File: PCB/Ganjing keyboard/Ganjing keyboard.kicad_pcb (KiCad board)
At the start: 2 copper layers, 304.8 x 122.8 mm, 172 parts, among them J1 Conn_01x04, J2 AVR-ISP-6, SW1 Rotary_Encoder_Switch, U1 ATmega32A-PU, Y1 Crystal

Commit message: Almost done routing clean up
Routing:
- net Net-(D48-Pad2): track 127.1 -> 130.2 mm

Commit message: Updating packages and reducing empty copper pours
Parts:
- moved C2 0.15 mm to (132.0, 121.7)
- moved C3 0.15 mm to (124.5, 119.2)
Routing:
- net Net-(D6-Pad2): track 87.6 -> 92.6 mm
- net Boot: track 114.4 -> 118.3 mm
- net Net-(D21-Pad2): track 66.7 -> 70.2 mm
- net row4: track 401.0 -> 404.3 mm
- net B1: track 295.2 -> 298.3 mm
- net B2: track 291.6 -> 294.5 mm
- net Net-(D41-Pad2): track 74.3 -> 71.7 mm
- net col13: track 302.1 -> 304.3 mm
- net col12: track 258.7 -> 260.9 mm
- net col11: track 254.8 -> 257.0 mm
- net col10: track 206.4 -> 208.6 mm
- net col9: track 246.2 -> 248.3 mm
- net col8: track 225.7 -> 227.8 mm
- net col7: track 197.3 -> 199.3 mm
- net col5: track 167.4 -> 169.5 mm
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
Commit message: Added remaining mounting holes
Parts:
- added REF10: MountingHole_2.2mm_M2_Pad, Keyboard:MountingHole_2.2mm_M2_Pad, F.Cu at (211.9, 205.6)
- added REF11: MountingHole_2.2mm_M2_Pad, Keyboard:MountingHole_2.2mm_M2_Pad, F.Cu at (304.6, 142.9)
- added REF12: MountingHole_2.2mm_M2_Pad, Keyboard:MountingHole_2.2mm_M2_Pad, F.Cu at (321.6, 199.7)
- added REF4: MountingHole_2.2mm_M2_Pad, Keyboard:MountingHole_2.2mm_M2_Pad, F.Cu at (0.00, 159.8)
- added REF7: MountingHole_2.2mm_M2_Pad, Keyboard:MountingHole_2.2mm_M2_Pad, F.Cu at (119.5, 142.9)
- added REF8: MountingHole_2.2mm_M2_Pad, Keyboard:MountingHole_2.2mm_M2_Pad, F.Cu at (102.3, 199.7)
- added REF9: MountingHole_2.2mm_M2_Pad, Keyboard:MountingHole_2.2mm_M2_Pad, F.Cu at (211.9, 142.9)
- moved D64 1.60 mm to (318.8, 198.6)
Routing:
- net Net-(D50-Pad2): track 111.8 -> 125.3 mm
- net Net-(D46-Pad2): track 143.1 -> 135.7 mm
- net Net-(D33-Pad2): track 112.5 -> 105.3 mm
- net row4: track 404.3 -> 405.9 mm
- net Net-(D64-Pad2): track 8.02 -> 9.62 mm

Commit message: Done adding via stitching
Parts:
- removed the REF4 at (0.00, 159.8)
- D68: value Caps lock -> Caps
- USB1: value USB_C_GCT_USB4085 -> USB_C_USB4085
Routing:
- net Net-(D17-Pad2): track 87.8 -> 93.1 mm
- net Net-(D32-Pad2): track 105.1 -> 108.9 mm
- net Net-(D67-Pad2): track 138.7 -> 142.5 mm
- net col8: track 227.8 -> 229.7 mm
- net col5: track 169.5 -> 171.4 mm
- net col9: track 248.3 -> 250.2 mm
- net col7: track 199.3 -> 201.3 mm
- net col4: track 145.0 -> 146.9 mm
- net col10: track 208.6 -> 210.5 mm
- net col11: track 257.0 -> 258.9 mm
- net Net-(D31-Pad2): track 138.3 -> 140.2 mm
- net col3: track 125.4 -> 127.2 mm
- net col6: track 222.9 -> 224.8 mm
- net col1: track 150.1 -> 148.8 mm
- net col2: track 136.7 -> 135.4 mm
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
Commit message: Changing footprint for crystal and adding some silk screen text
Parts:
- D68: value Caps -> Caps lock
- USB1: value USB_C_USB4085 -> USB_C_GCT_USB4085
- Y1: footprint Keyboard:Crystal_HC49-4H_Vertical -> GanJing-crystal:CTS-ATS16B-0
- moved Y1 2.35 mm to (139.3, 120.4)
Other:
- board text added: "Designed by Mingze Jin"
- board text added: "GanJing Keyboard prototype"

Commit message: Fixing some silk screen stuff on the PCB
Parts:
- D68: value Caps lock -> Caps
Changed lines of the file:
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@@
     (add_net row4)
   )
+  (module Rotary_Encoder:RotaryEncoder_Alps_EC11E-Switch_Vertical_H20mm (layer F.Cu)
+    (at 352.425 140.49375 90)
+    (descr "Alps rotary encoder, EC12E... with switch, vertical shaft, http://www.alps.com/prod/info/E/HTML/Encoder/Incremental/EC11/EC11E15204A3.html")
+    (tags "rotary encoder")
+    (fp_text reference SW1 (at 2.8 -4.7 90) (layer F.SilkS)
+      (effects (font (size 1 1) (thickness 0.15)))
+    )
+    (fp_text value Rotary_Encoder_Switch (at 7.5 10.4 90) (layer F.Fab)
+      (effects (font (size 1 1) (thickness 0.15)))
+    )
+    (fp_circle (center 7.5 2.5) (end 10.5 2.5) (layer F.Fab) (width 0.12))
+    (fp_circle (center 7.5 2.5) (end 10.5 2.5) (layer F.Fab) (width 0.12))
+    (fp_line (start 16 9.6) (end -1.5 9.6) (layer F.CrtYd) (width 0.05))
+    (fp_line (start 16 9.6) (end 16 -4.6) (layer F.CrtYd) (width 0.05))
+    (fp_line (start -1.5 -4.6) (end -1.5 9.6) (layer F.CrtYd) (width 0.05))
+    (fp_line (start -1.5 -4.6) (end 16 -4.6) (layer F.CrtYd) (width 0.05))
+    (fp_line (start 2.5 -3.3) (end 13.5 -3.3) (layer F.Fab) (width 0.12))
+    (fp_line (start 13.5 -3.3) (end 13.5 8.3) (layer F.Fab) (width 0.12))
+    (fp_line (start 13.5 8.3) (end 1.5 8.3) (layer F.Fab) (width 0.12))
+    (fp_line (start 1.5 8.3) (end 1.5 -2.2) (layer F.Fab) (width 0.12))
+    (fp_line (start 1.5 -2.2) (end 2.5 -3.3) (layer F.Fab) (width 0.12))
+    (fp_line (start 9.5 -3.4) (end 13.6 -3.4) (layer F.Fab) (width 0.12))
+    (fp_line (start 13.6 8.4) (end 9.5 8.4) (layer F.Fab) (width 0.12))
+    (fp_line (start 5.5 8.4) (end 1.4 8.4) (layer F.Fab) (width 0.12))
+    (fp_line (start 5.5 -3.4) (end 1.4 -3.4) (layer F.Fab) (width 0.12))
+    (fp_line (start 1.4 -3.4) (end 1.4 8.4) (layer F.Fab) (width 0.12))
+    (fp_line (start 0 -1.3) (end -0.3 -1.6) (layer F.SilkS) (width 0.12))
+    (fp_line (start -0.3 -1.6) (end 0.3 -1.6) (layer F.SilkS) (width 0.12))
+    (fp_line (start 0.3 -1.6) (end 0 -1.3) (layer F.SilkS) (width 0.12))
+    (fp_line (start 7.5 -0.5) (end 7.5 5.5) (layer F.Fab) (width 0.12))
+    (fp_line (start 4.5 2.5) (end 10.5 2.5) (layer F.Fab) (width 0.12))
+    (fp_line (start 13.6 -3.4) (end 13.6 -1) (layer F.Fab) (width 0.12))
+    (fp_line (start 13.6 1.2) (end 13.6 3.8) (layer F.Fab) (width 0.12))
+    (fp_line (start 13.6 6) (end 13.6 8.4) (layer F.Fab) (width 0.12))
+    (fp_line (start 7.5 2) (end 7.5 3) (layer F.Fab) (width 0.12))
+    (fp_line (start 7 2.5) (end 8 2.5) (layer F.Fab) (width 0.12))
+    (fp_text user %R (at 11.1 6.3 90) (layer F.Fab)
+      (effects (font (size 1 1) (thickness 0.15)))
+    )
+    (pad A thru_hole rect (at 0 0 90) (size 2 2) (drill 1) (layers *.Cu *.Mask)
+      (net 111 B2))
+    (pad C thru_hole circle (at 0 2.5 90) (size 2 2) (drill 1) (layers *.Cu *.Mask)
+      (net 1 GND))
+    (pad B thru_hole circle (at 0 5 90) (size 2 2) (drill 1) (layers *.Cu *.Mask)
+      (net 112 B1))
+    (pad MP thru_hole rect (at 7.5 -3.1 90) (size 3.2 2) (drill oval 2.8 1.5) (layers *.Cu *.Mask))
+    (pad MP thru_hole rect (at 7.5 8.1 90) (size 3.2 2) (drill oval 2.8 1.5) (layers *.Cu *.Mask))
+    (pad S2 thru_hole circle (at 14.5 0 90) (size 2 2) (drill 1) (layers *.Cu *.Mask)
+      (net 20 SW15B))
+    (pad S1 thru_hole circle (at 14.5 5 90) (size 2 2) (drill 1) (layers *.Cu *.Mask)
+      (net 103 SW15A))
+    (model ${KISYS3DMOD}/Rotary_Encoder.3dshapes/RotaryEncoder_Alps_EC11E-Switch_Vertical_H20mm.wrl
+      (at (xyz 0 0 0))
+      (scale (xyz 1 1 1))
+      (rotate (xyz 0 0 0))
+    )
+  )
+  (module "Keyboard:ssd1306 128x32 oled" (layer F.Cu)
+    (at 269.08125 209.55)
+    (fp_text reference J1 (at 0 0.5) (layer F.SilkS)
+      (effects (font (size 1 1) (thickness 0.15)))
+    )
+    (fp_text value Conn_01x04 (at 0 -0.5) (layer F.Fab)
+      (effects (font (size 1 1) (thickness 0.15)))
+    )
+    (fp_line (start -14 6) (end -14 -6) (layer F.Fab) (width 0.15))
+    (fp_line (start 19 6) (end 19 -6) (layer F.Fab) (width 0.15))
+    (fp_line (start -19 6) (end -19 -6) (layer F.Fab) (width 0.15))
+    (fp_line (start -19 6) (end 19 6) (layer F.Fab) (width 0.15))
+    (fp_line (start -19 -6) (end 19 -6) (layer F.Fab) (width 0.15))
+    (pad 1 thru_hole circle (at -17.5 3.81) (size 1.524 1.524) (drill 0.762) (layers *.Cu *.Mask)
+      (net 83 SDA))
+    (pad 2 thru_hole circle (at -17.5 1.27) (size 1.524 1.524) (drill 0.762) (layers *.Cu *.Mask)
+      (net 84 SCL))
+    (pad 3 thru_hole circle (at -17.5 -1.27) (size 1.524 1.524) (drill 0.762) (layers *.Cu *.Mask)
+      (net 82 VCC))
+    (pad 4 thru_hole circle (at -17.5 -3.81) (size 1.524 1.524) (drill 0.762) (layers *.Cu *.Mask)
+      (net 1 GND))
+  )
   (module GanJing-crystal:CTS-ATS16B-0 (layer F.Cu)
     (at 139.3 120.4 180)
@@
     (pad 1 thru_hole circle (at 0 0) (size 4.4 4.4) (drill 2.2) (layers *.Cu *.Mask))
   )
-  (module Rotary_Encoder:RotaryEncoder_Alps_EC11E-Switch_Vertical_H20mm (layer F.Cu)
-    (at 352.425 140.49375 90)
-    (descr "Alps rotary encoder, EC12E... with switch, vertical shaft, http://www.alps.com/prod/info/E/HTML/Encoder/Incremental/EC11/EC11E15204A3.html")
-    (tags "rotary encoder")
-    (fp_text reference SW1 (at 2.8 -4.7 90) (layer F.SilkS)
-      (effects (font (size 1 1) (thickness 0.15)))
-    )
-    (fp_text value Rotary_Encoder_Switch (at 7.5 10.4 90) (layer F.Fab)
-      (effects (font (size 1 1) (thickness 0.15)))
-    )
-    (fp_circle (center 7.5 2.5) (end 10.5 2.5) (layer F.Fab) (width 0.12))
-    (fp_circle (center 7.5 2.5) (end 10.5 2.5) (layer F.SilkS) (width 0.12))
-    (fp_line (start 16 9.6) (end -1.5 9.6) (layer F.CrtYd) (width 0.05))
-    (fp_line (start 16 9.6) (end 16 -4.6) (layer F.CrtYd) (width 0.05))
-    (fp_line (start -1.5 -4.6) (end -1.5 9.6) (layer F.CrtYd) (width 0.05))
-    (fp_line (start -1.5 -4.6) (end 16 -4.6) (layer F.CrtYd) (width 0.05))
-    (fp_line (start 2.5 -3.3) (end 13.5 -3.3) (layer F.Fab) (width 0.12))
-    (fp_line (start 13.5 -3.3) (end 13.5 8.3) (layer F.Fab) (width 0.12))
-    (fp_line (start 13.5 8.3) (end 1.5 8.3) (layer F.Fab) (width 0.12))
-    (fp_line (start 1.5 8.3) (end 1.5 -2.2) (layer F.Fab) (width 0.12))
-    (fp_line (start 1.5 -2.2) (end 2.5 -3.3) (layer F.Fab) (width 0.12))
-    (fp_line (start 9.5 -3.4) (end 13.6 -3.4) (layer F.SilkS) (width 0.12))
-    (fp_line (start 13.6 8.4) (end 9.5 8.4) (layer F.SilkS) (width 0.12))
-    (fp_line (start 5.5 8.4) (end 1.4 8.4) (layer F.SilkS) (width 0.12))
-    (fp_line (start 5.5 -3.4) (end 1.4 -3.4) (layer F.SilkS) (width 0.12))
-    (fp_line (start 1.4 -3.4) (end 1.4 8.4) (layer F.SilkS) (width 0.12))
-    (fp_line (start 0 -1.3) (end -0.3 -1.6) (layer F.SilkS) (width 0.12))
-    (fp_line (start -0.3 -1.6) (end 0.3 -1.6) (layer F.SilkS) (width 0.12))
-    (fp_line (start 0.3 -1.6) (end 0 -1.3) (layer F.SilkS) (width 0.12))
-    (fp_line (start 7.5 -0.5) (end 7.5 5.5) (layer F.Fab) (width 0.12))
-    (fp_line (start 4.5 2.5) (end 10.5 2.5) (layer F.Fab) (width 0.12))
-    (fp_line (start 13.6 -3.4) (end 13.6 -1) (layer F.SilkS) (width 0.12))
-    (fp_line (start 13.6 1.2) (end 13.6 3.8) (layer F.SilkS) (width 0.12))
-    (fp_line (start 13.6 6) (end 13.6 8.4) (layer F.SilkS) (width 0.12))
-    (fp_line (start 7.5 2) (end 7.5 3) (layer F.SilkS) (width 0.12))
-    (fp_line (start 7 2.5) (end 8 2.5) (layer F.SilkS) (width 0.12))
-    (fp_text user %R (at 11.1 6.3 90) (layer F.Fab)
-      (effects (font (size 1 1) (thickness 0.15)))
-    )
-    (pad A thru_hole rect (at 0 0 90) (size 2 2) (drill 1) (layers *.Cu *.Mask)
-      (net 111 B2))
-    (pad C thru_hole circle (at 0 2.5 90) (size 2 2) (drill 1) (layers *.Cu *.Mask)
-      (net 1 GND))
-    (pad B thru_hole circle (at 0 5 90) (size 2 2) (drill 1) (layers *.Cu *.Mask)
-      (net 112 B1))
-    (pad MP thru_hole rect (at 7.5 -3.1 90) (size 3.2 2) (drill oval 2.8 1.5) (layers *.Cu *.Mask))
-    (pad MP thru_hole rect (at 7.5 8.1 90) (size 3.2 2) (drill oval 2.8 1.5) (layers *.Cu *.Mask))
-    (pad S2 thru_hole circle (at 14.5 0 90) (size 2 2) (drill 1) (layers *.Cu *.Mask)
-      (net 20 SW15B))
-    (pad S1 thru_hole circle (at 14.5 5 90) (size 2 2) (drill 1) (layers *.Cu *.Mask)
-      (net 103 SW15A))
-    (model ${KISYS3DMOD}/Rotary_Encoder.3dshapes/RotaryEncoder_Alps_EC11E-Switch_Vertical_H20mm.wrl
-      (at (xyz 0 0 0))
-      (scale (xyz 1 1 1))
-      (rotate (xyz 0 0 0))
-    )
-  )
   (module MX_Only:MXOnly-1.5U-NoLED (layer F.Cu)
     (at 330.99375 152.4)
@@
     )
   )
-  (module "Keyboard:ssd1306 128x32 oled" (layer F.Cu)
-    (at 269.08125 209.55)
-    (fp_text reference J1 (at 0 0.5) (layer F.SilkS)
-      (effects (font (size 1 1) (thickness 0.15)))
-    )
-    (fp_text value Conn_01x04 (at 0 -0.5) (layer F.Fab)
-      (effects (font (size 1 1) (thickness 0.15)))
-    )
-    (fp_line (start -14 6) (end -14 -6) (layer F.SilkS) (width 0.15))
-    (fp_line (start 19 6) (end 19 -6) (layer F.SilkS) (width 0.15))
-    (fp_line (start -19 6) (end -19 -6) (layer F.SilkS) (width 0.15))
-    (fp_line (start -19 6) (end 19 6) (layer F.SilkS) (width 0.15))
-    (fp_line (start -19 -6) (end 19 -6) (layer F.SilkS) (width 0.15))
-    (pad 1 thru_hole circle (at -17.5 3.81) (size 1.524 1.524) (drill 0.762) (layers *.Cu *.Mask)
-      (net 83 SDA))
-    (pad 2 thru_hole circle (at -17.5 1.27) (size 1.524 1.524) (drill 0.762) (layers *.Cu *.Mask)
-      (net 84 SCL))
-    (pad 3 thru_hole circle (at -17.5 -1.27) (size 1.524 1.524) (drill 0.762) (layers *.Cu *.Mask)
-      (net 82 VCC))
-    (pad 4 thru_hole circle (at -17.5 -3.81) (size 1.524 1.524) (drill 0.762) (layers *.Cu *.Mask)
-      (net 1 GND))
-  )
   (module Keyboard:polyfuse_5.1mm (layer F.Cu)
     (at 84.2 112)
@@
       (effects (font (size 1 1) (thickness 0.15)))
     )
-    (fp_text value "Caps lock" (at 7.5 -1.1) (layer F.SilkS)
+    (fp_text value Caps (at 7.5 -1.1) (layer F.SilkS)
       (effects (font (size 1.5 1.5) (thickness 0.25)))
     )

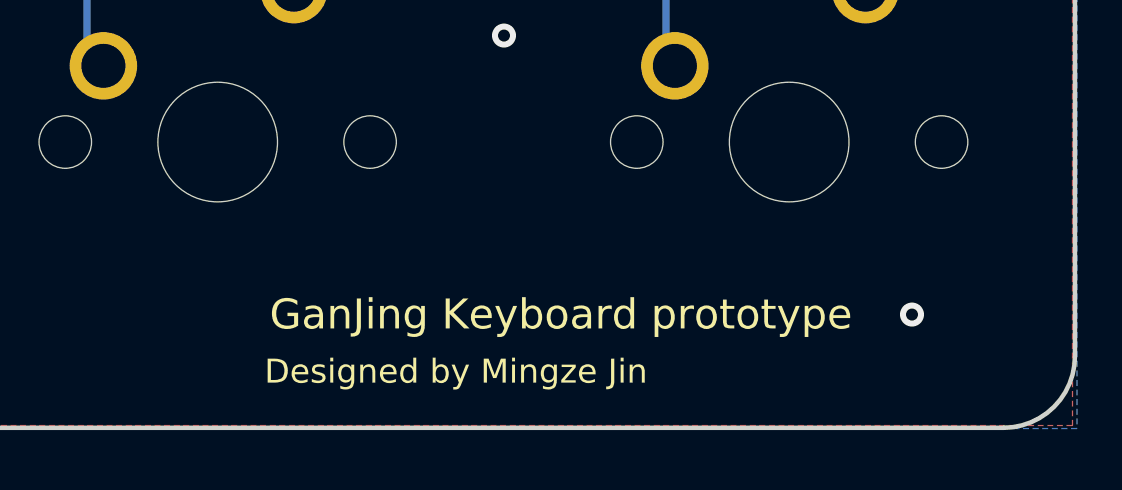
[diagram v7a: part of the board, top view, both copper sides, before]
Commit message: Minor mistake in text
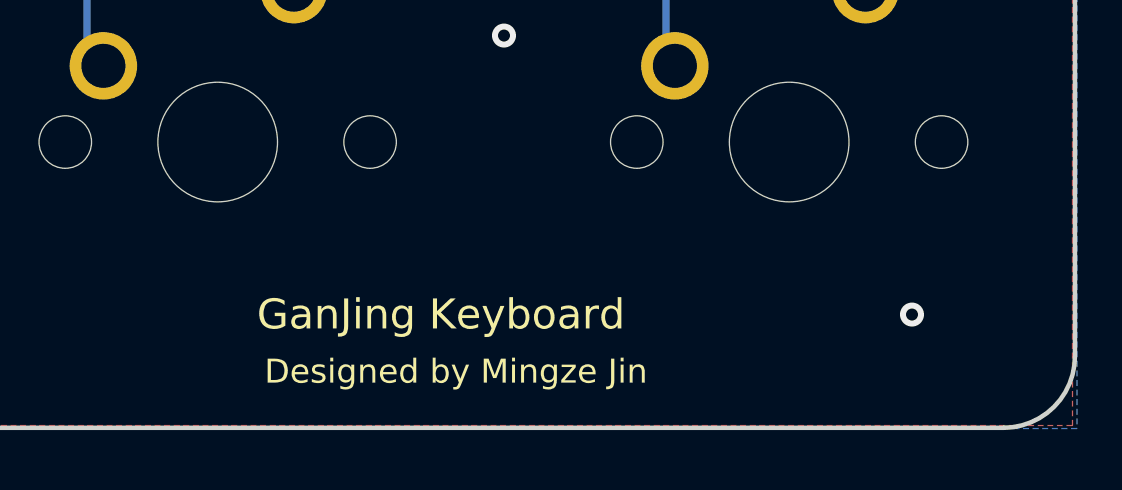
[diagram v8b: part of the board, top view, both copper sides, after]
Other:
- board text added: "GanJing Keyboard"
- board text removed: "GanJing Keyboard prototype"
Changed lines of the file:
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@@
   (page A3)
   (layers
-    (0 F.Cu signal)
-    (31 B.Cu signal)
+    (0 F.Cu signal hide)
+    (31 B.Cu signal hide)
     (32 B.Adhes user)
     (33 F.Adhes user)
@@
     (effects (font (size 0.8 0.8) (thickness 0.15)))
   )
-  (gr_text "GanJing Keyboard prototype" (at 347.2 215.3) (layer F.SilkS)
+  (gr_text "GanJing Keyboard" (at 343.2 215.3) (layer F.SilkS)
     (effects (font (size 1 1) (thickness 0.15)))
   )
